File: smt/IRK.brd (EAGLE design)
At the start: 142.9 x 39.7 mm, 37 parts, among them IC1 PIC18F25K50, IC2 MAX4066ESD, Q1 MMBT2222A, Q2 MMBT3906, U1 TSOP4838

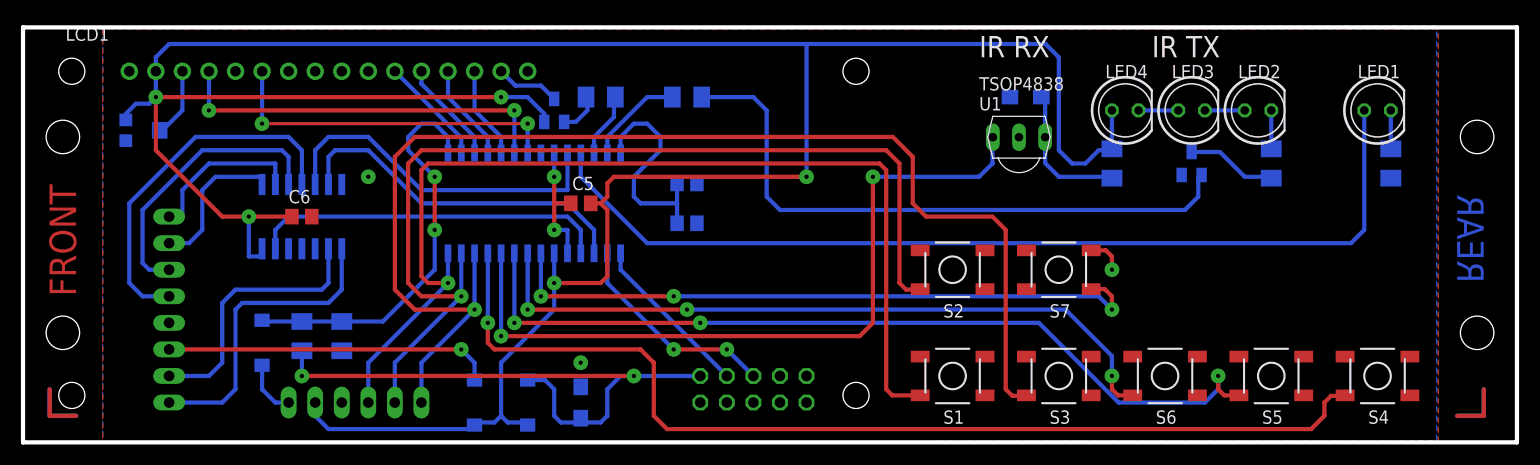
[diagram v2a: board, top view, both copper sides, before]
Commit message: Replaced old 2550 device with P18F25K50 in IRK.lbr
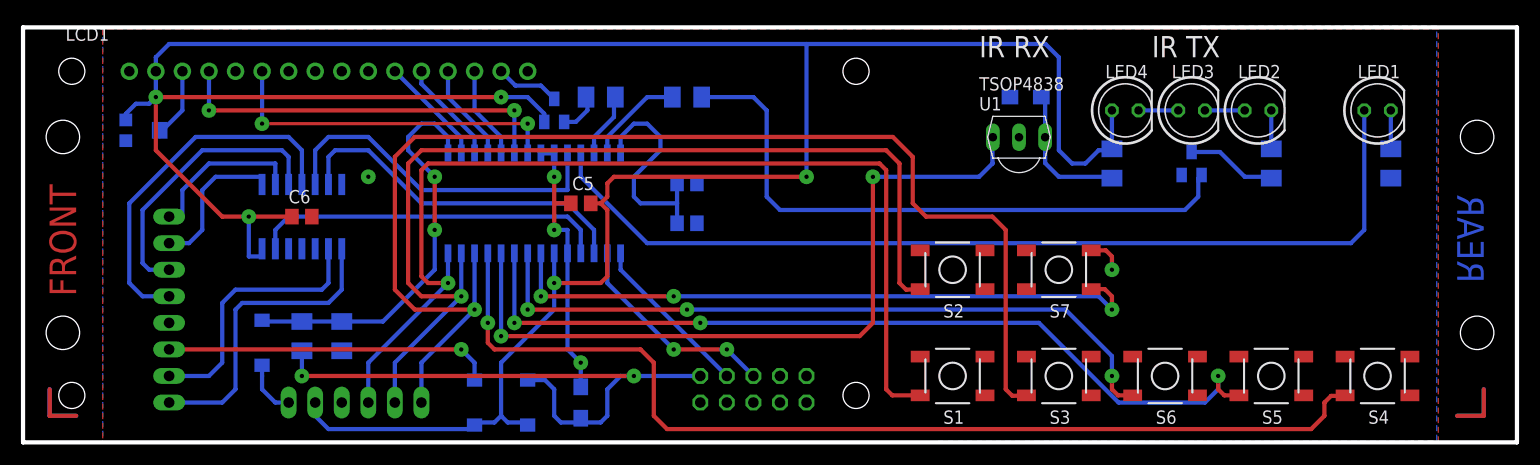
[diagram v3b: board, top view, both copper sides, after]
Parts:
- IC1: device microchip:SO28W -> irk:SO28W
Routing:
- net GND: track 15.9 -> 30.5 mm

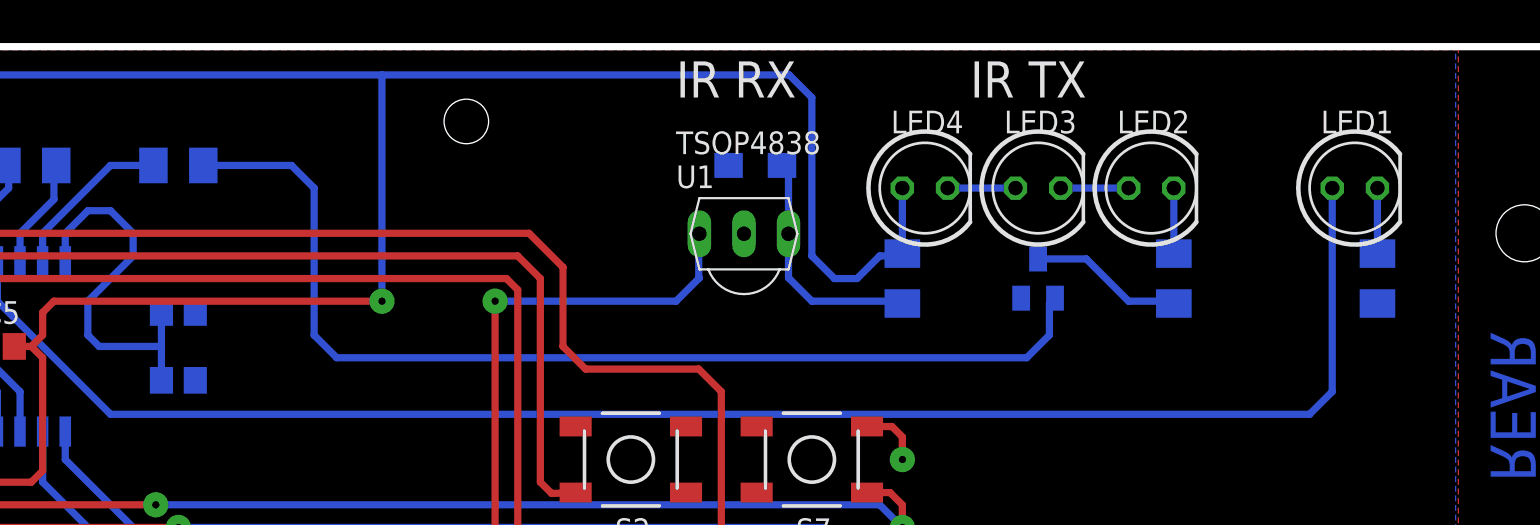
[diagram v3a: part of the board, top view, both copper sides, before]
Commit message: Spaced the holes for the IR TX and Activity LEDs at 0.1 inch intervals.
Now (if you want) you can solder a 12x1 pin socket header and plug
your IR TX and Activity LEDs into it rather than soldering them
directly to the board. Long term reliability might be an issue
as the leads oxidise though. The interspersed pin sockets appear on
the schematic as grounded 1x1 header pins.

The IR RX LED has remained slightly offset from the others, because it
needs to be bent 90° so that it is perpendicular to the board.

The board version is now 2.01 as a result of these minor layout changes
and the Gerber files have been regenerated.
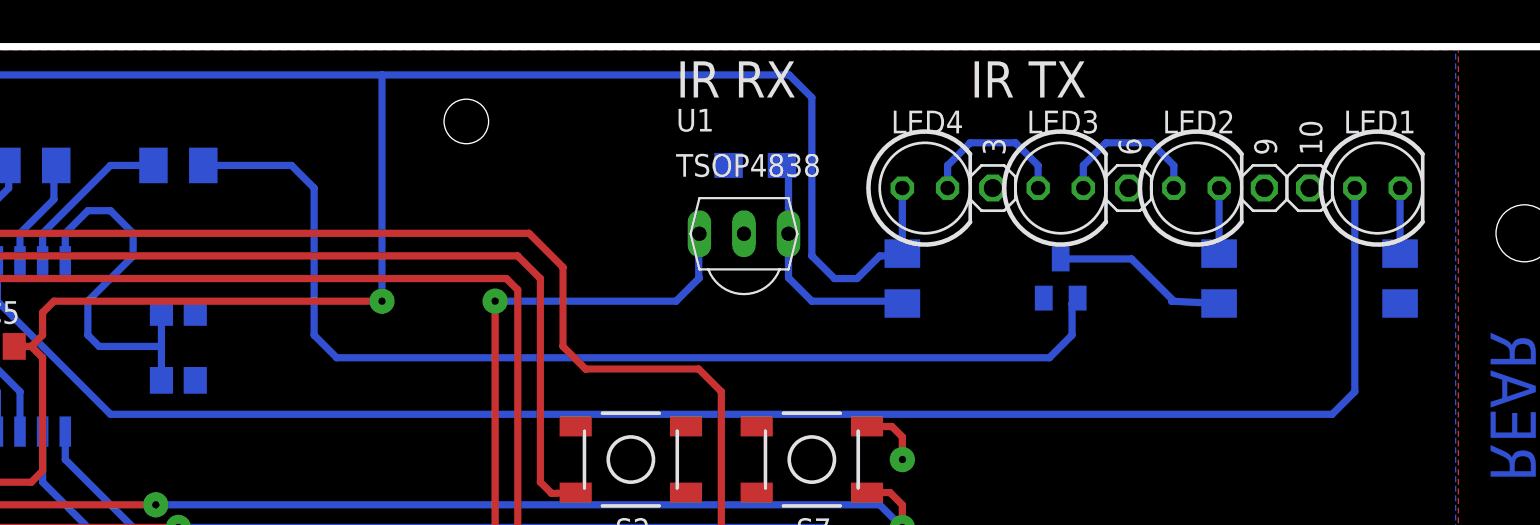
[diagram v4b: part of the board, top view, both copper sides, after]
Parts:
- added 10, 3, 6, 9: (no value), pinhead:1X01
- moved LED2 2.54 mm to (120.7, 31.8)
- moved R4 2.54 mm to (121.9, 26.7)
- moved LED1 1.27 mm to (130.8, 31.8)
- moved R3 1.27 mm to (132.1, 26.7)
- moved LED3 1.27 mm to (113.0, 31.8)
- moved Q1 1.27 mm to (113.0, 26.7)
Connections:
- net GND: now also 10.1, 3.1, 6.1, 9.1
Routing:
- net N$27: track 3.81 -> 8.67 mm
- net N$26: track 3.81 -> 8.67 mm
- net N$30: track 8.66 -> 10.1 mm
- net N$29: track 59.5 -> 60.8 mm
- net N$46: track 91.8 -> 93.0 mm
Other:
- board text added: "IRK! v2.01 USB Infrared Keyboard (C) 2010-2014 androidarmstrong@gmail.com"
- board text removed: "IRK! v2.0 USB Infrared Keyboard (C) 2010-2014 androidarmstrong@gmail.com"
